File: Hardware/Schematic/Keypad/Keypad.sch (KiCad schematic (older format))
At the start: 9 parts, among them J9 Conn_01x02, U1 TCA8418RTWR

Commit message: Split-up schematics into three seperate projects with a parts library as well
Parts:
- U1: symbol TCA8418RTWR:TCA8418RTWR -> parts:TCA8418RTWR-TCA8418RTWR
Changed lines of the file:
@@
 EESchema Schematic File Version 4
-LIBS:WiFiLMR-cache
 EELAYER 29 0
 EELAYER END
 $Descr A4 11693 8268
 encoding utf-8
-Sheet 4 6
+Sheet 1 1
 Title ""
 Date ""
@@
 	2450 3200 2300 3200
 $Comp
-L TCA8418RTWR:TCA8418RTWR U?
+L parts:TCA8418RTWR-TCA8418RTWR U1
 U 1 1 5D178EB2
 P 3150 3300
-AR Path="/5D178EB2" Ref="U?"  Part="1"
+AR Path="/5D178EB2" Ref="U1"  Part="1"
 AR Path="/5D1772AD/5D178EB2" Ref="U1"  Part="1"
 F 0 "U1" H 3150 4270 50  0000 C CNN

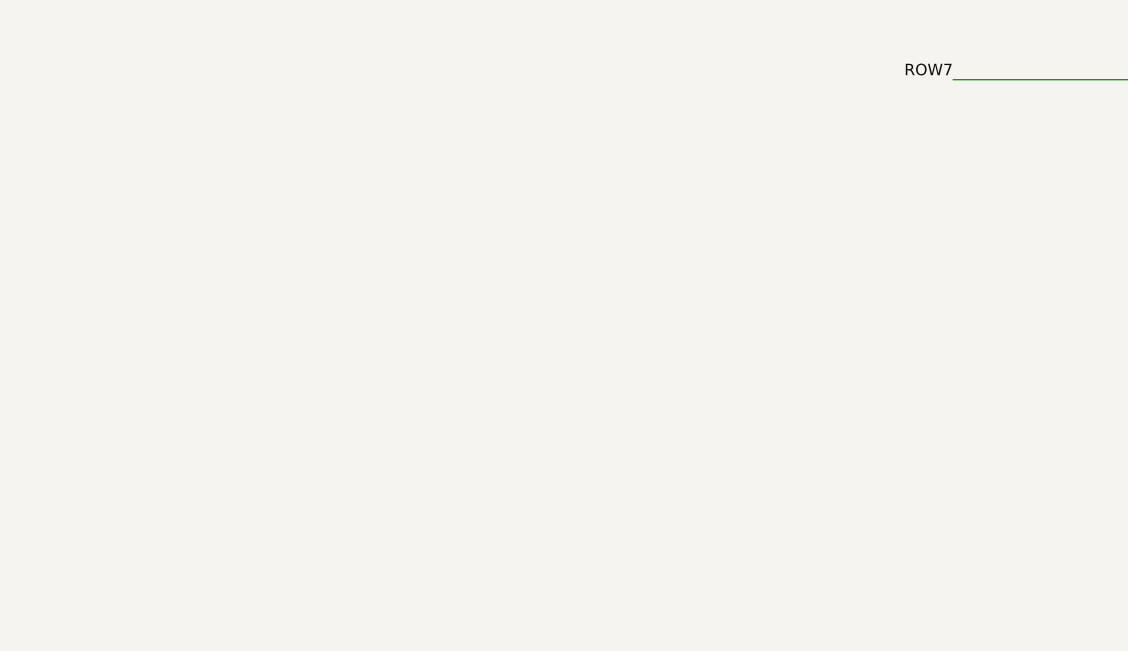
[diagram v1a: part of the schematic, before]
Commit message: Updated keypad and display schematic to use header sockets for intra-board connections.
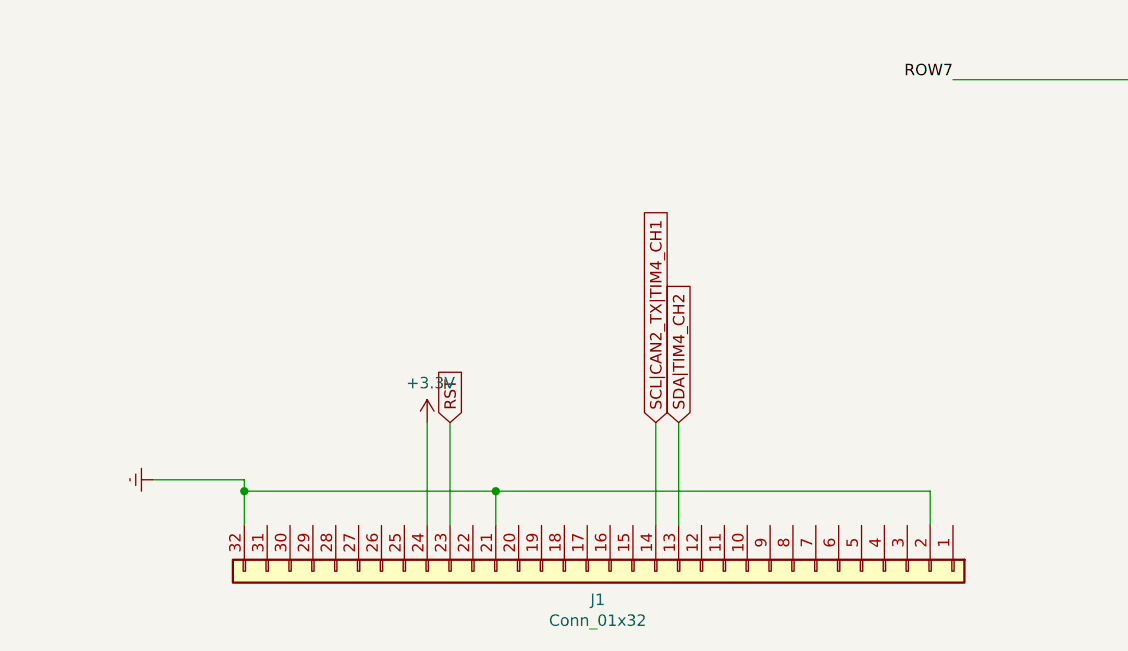
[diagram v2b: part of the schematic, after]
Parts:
- added J1: Conn_01x32, Connector_PinSocket_2.54mm:PinSocket_2x16_P2.54mm_Horizontal, symbol Connector_Generic:Conn_01x32
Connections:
- net +3V3: now also J1.24 (Pin_24)
- net Earth: now also J1.2 (Pin_2), J1.21 (Pin_21), J1.32 (Pin_32)
- net RST: now also J1.23 (Pin_23)
- net SCL|CAN2_TX|TIM4_CH1: now also J1.14 (Pin_14)
- net SDA|TIM4_CH2: now also J1.13 (Pin_13)
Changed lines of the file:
@@
 EESchema Schematic File Version 4
+LIBS:Keypad-cache
 EELAYER 29 0
 EELAYER END
@@
 Text GLabel 2300 2900 0    50   BiDi ~ 0
 RST
+$Comp
+L Connector_Generic:Conn_01x32 J1
+U 1 1 5D05A1AD
+P 3750 7350
+F 0 "J1" V 3875 7296 50  0000 C CNN
+F 1 "Conn_01x32" V 3966 7296 50  0000 C CNN
+F 2 "Connector_PinSocket_2.54mm:PinSocket_2x16_P2.54mm_Horizontal" H 3750 7350 50  0001 C CNN
+F 3 "~" H 3750 7350 50  0001 C CNN
+	1    3750 7350
+	0    1    1    0
+$EndComp
+$Comp
+L power:Earth #PWR0101
+U 1 1 5D05DF38
+P 1750 6950
+F 0 "#PWR0101" H 1750 6700 50  0001 C CNN
+F 1 "Earth" H 1750 6800 50  0001 C CNN
+F 2 "" H 1750 6950 50  0001 C CNN
+F 3 "~" H 1750 6950 50  0001 C CNN
+	1    1750 6950
+	0    1    1    0
+$EndComp
+Wire Wire Line
+	2150 7150 2150 7000
+Wire Wire Line
+	2150 6950 1750 6950
+Wire Wire Line
+	2150 7000 3250 7000
+Wire Wire Line
+	3250 7000 3250 7150
+Connection ~ 2150 7000
+Wire Wire Line
+	2150 7000 2150 6950
+Wire Wire Line
+	3250 7000 5150 7000
+Wire Wire Line
+	5150 7000 5150 7150
+Connection ~ 3250 7000
+$Comp
+L power:+3.3V #PWR0102
+U 1 1 5D061ED3
+P 2950 6700
+F 0 "#PWR0102" H 2950 6550 50  0001 C CNN
+F 1 "+3.3V" H 2965 6873 50  0000 C CNN
+F 2 "" H 2950 6700 50  0001 C CNN
+F 3 "" H 2950 6700 50  0001 C CNN
+	1    2950 6700
+	1    0    0    -1
+$EndComp
+Wire Wire Line
+	2950 7150 2950 6700
+Wire Wire Line
+	3050 7150 3050 6700
+Wire Wire Line
+	3950 7150 3950 6700
+Wire Wire Line
+	4050 7150 4050 6700
+Text GLabel 3050 6700 1    50   Input ~ 0
+RST
+Text GLabel 3950 6700 1    50   Input ~ 0
+SCL|CAN2_TX|TIM4_CH1
+Text GLabel 4050 6700 1    50   Input ~ 0
+SDA|TIM4_CH2
 $EndSCHEMATC

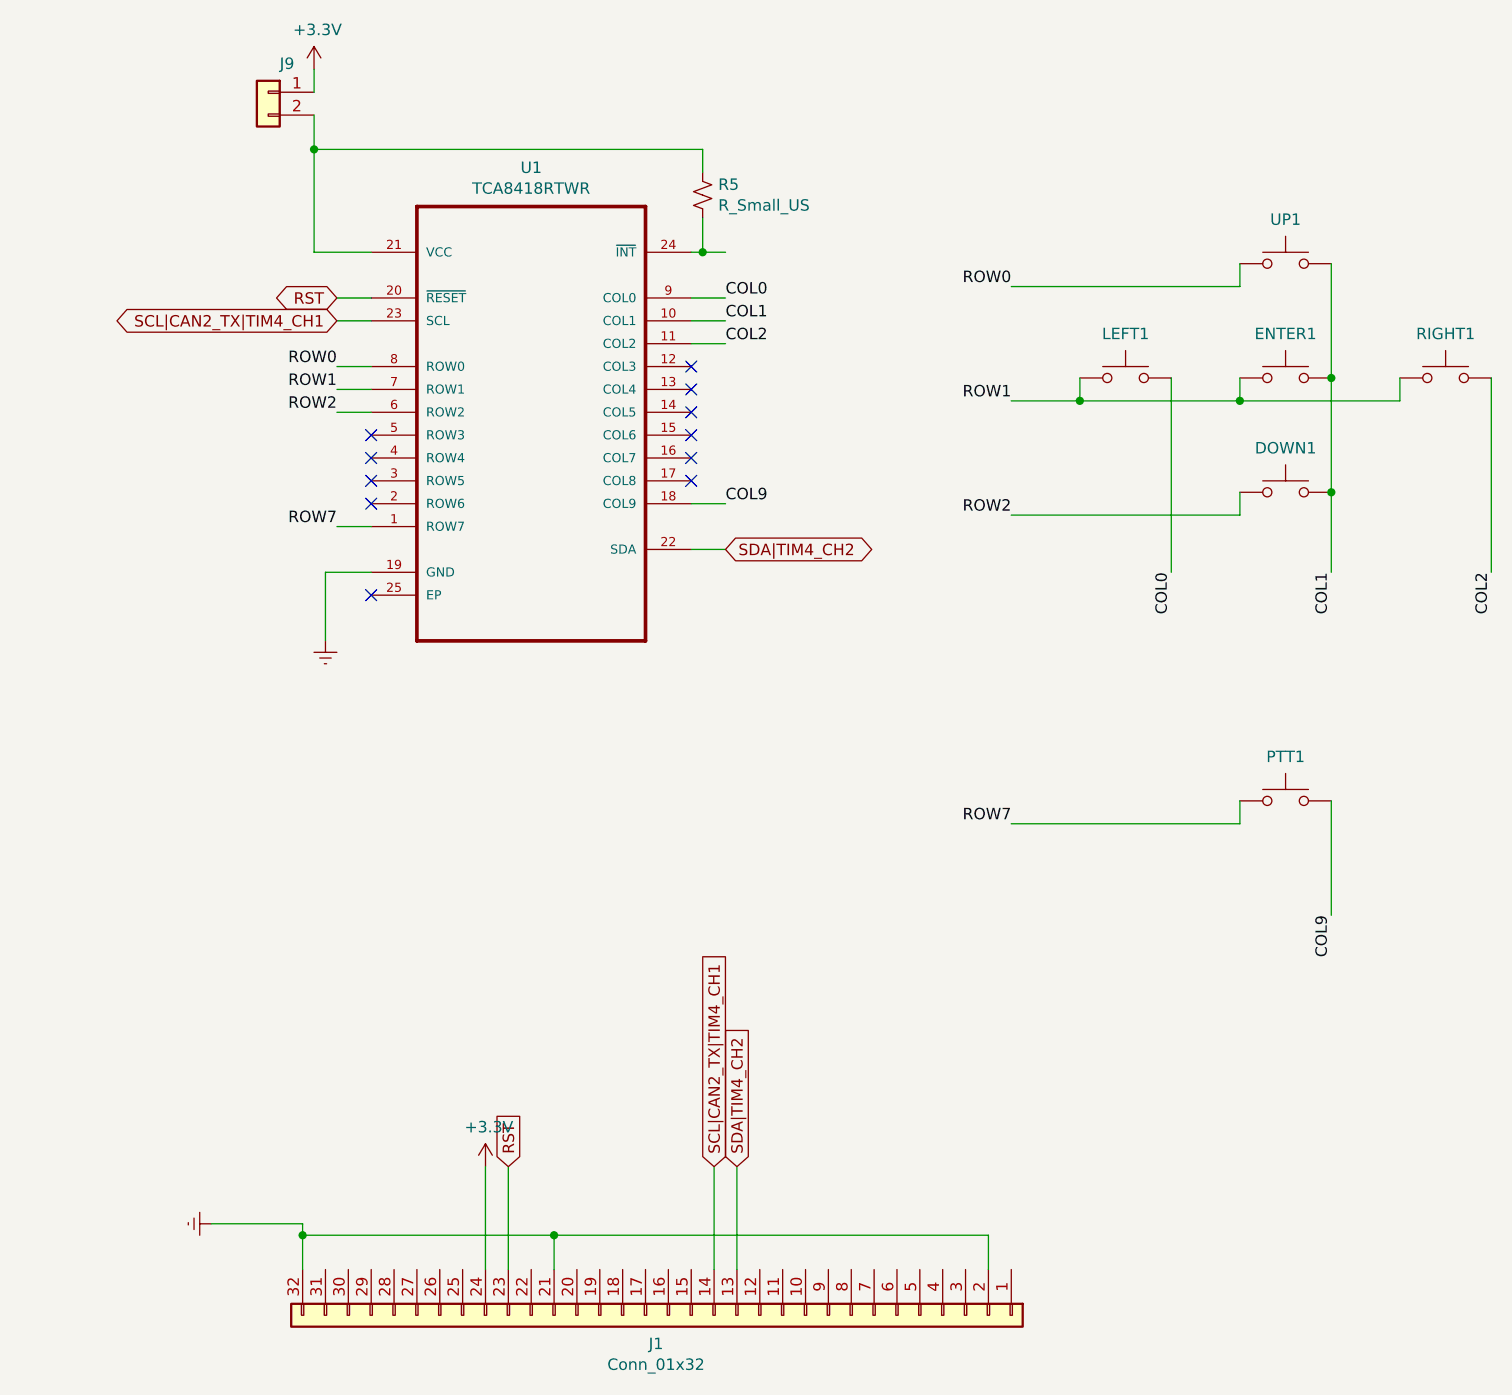
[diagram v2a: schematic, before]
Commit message: Added male 02x16 header to auxillary boards so they can be "stacked" together
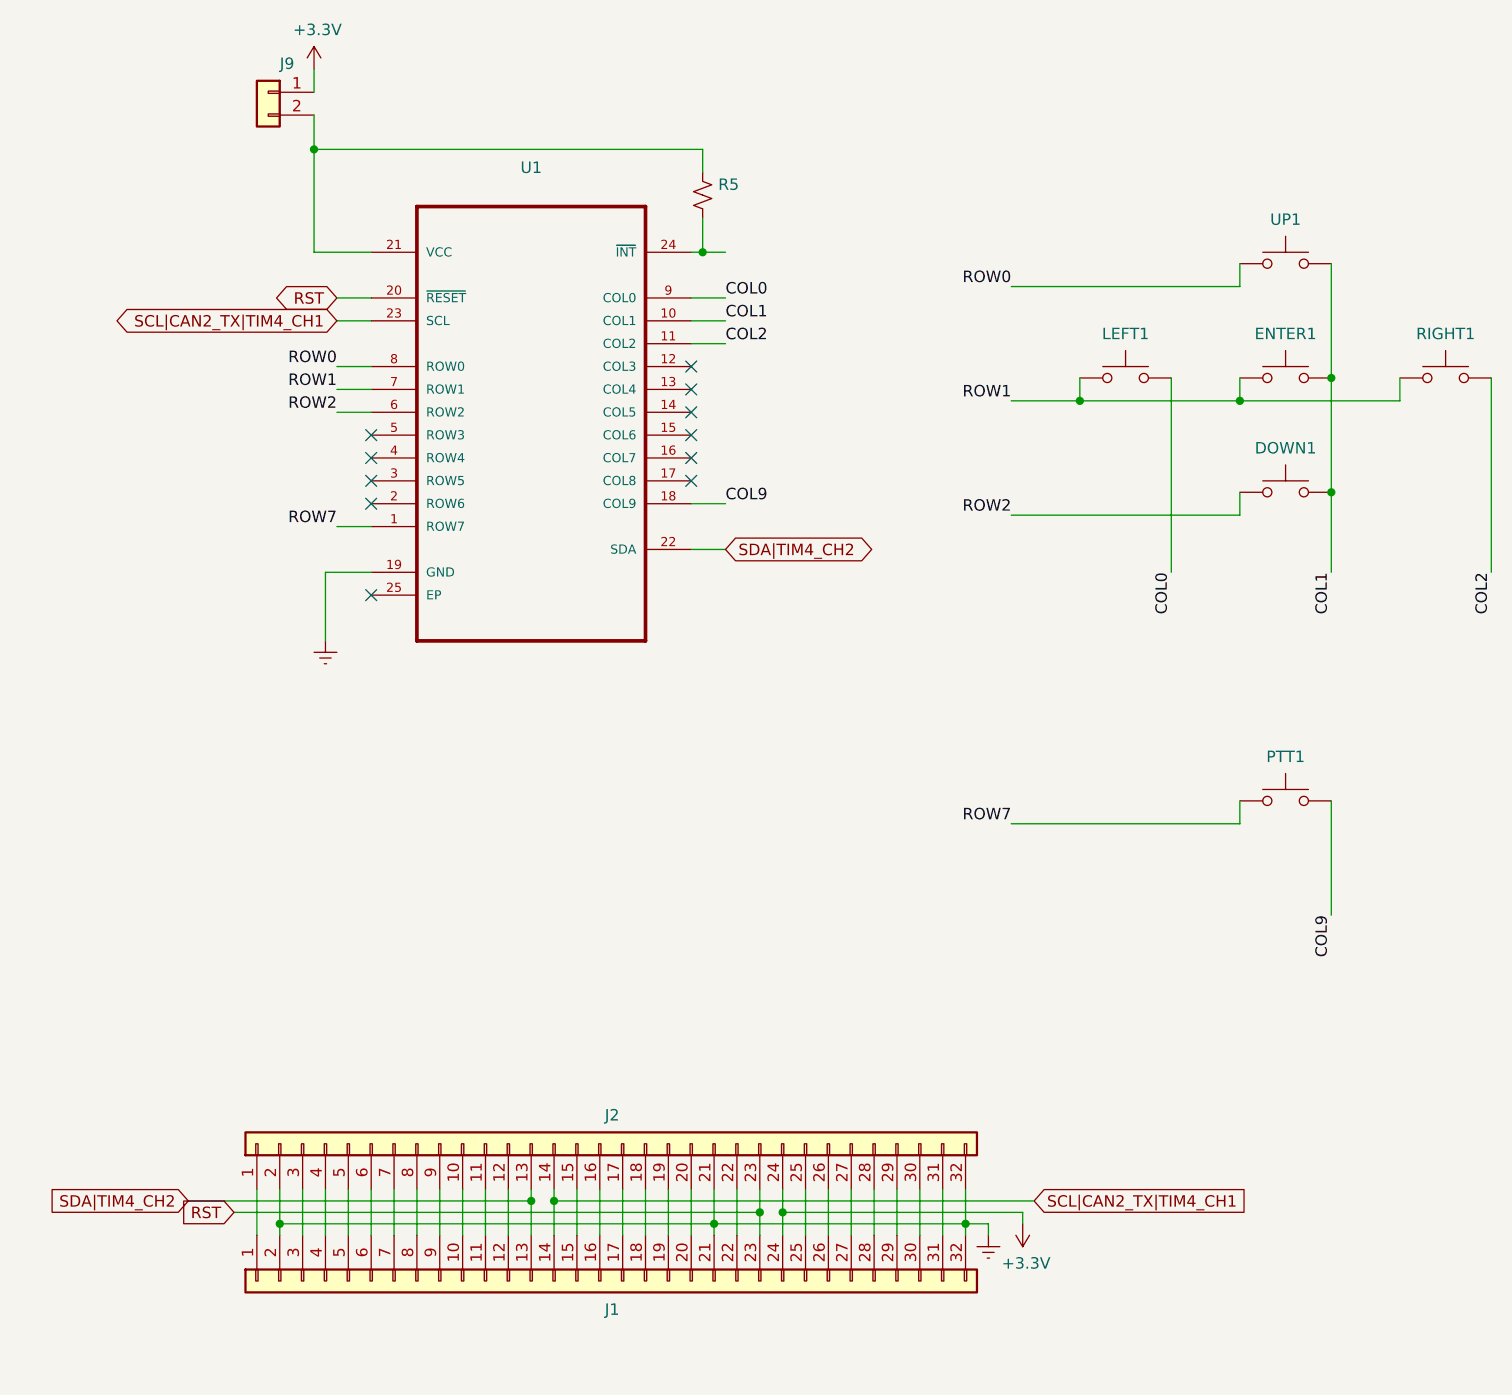
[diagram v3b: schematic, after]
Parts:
- added J2: Conn_01x32, Connector_PinHeader_2.54mm:PinHeader_2x16_P2.54mm_Horizontal, symbol Connector_Generic:Conn_01x32
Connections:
- net +3V3: now also J2.24 (Pin_24)
- net Earth: now also J2.2 (Pin_2), J2.21 (Pin_21), J2.32 (Pin_32)
- net RST: now also J2.23 (Pin_23)
- net SCL|CAN2_TX|TIM4_CH1: now also J2.14 (Pin_14)
- net SDA|TIM4_CH2: now also J2.13 (Pin_13)
- net at J1.1 (Pin_1): now also J2.1 (Pin_1)
- net at J1.10 (Pin_10): now also J2.10 (Pin_10)
- net at J1.11 (Pin_11): now also J2.11 (Pin_11)
- net at J1.12 (Pin_12): now also J2.12 (Pin_12)
- net at J1.15 (Pin_15): now also J2.15 (Pin_15)
- net at J1.16 (Pin_16): now also J2.16 (Pin_16)
- net at J1.17 (Pin_17): now also J2.17 (Pin_17)
- net at J1.18 (Pin_18): now also J2.18 (Pin_18)
- net at J1.19 (Pin_19): now also J2.19 (Pin_19)
- net at J1.20 (Pin_20): now also J2.20 (Pin_20)
- net at J1.22 (Pin_22): now also J2.22 (Pin_22)
- net at J1.25 (Pin_25): now also J2.25 (Pin_25)
- net at J1.26 (Pin_26): now also J2.26 (Pin_26)
- net at J1.27 (Pin_27): now also J2.27 (Pin_27)
- net at J1.28 (Pin_28): now also J2.28 (Pin_28)
- net at J1.29 (Pin_29): now also J2.29 (Pin_29)
- net at J1.3 (Pin_3): now also J2.3 (Pin_3)
- net at J1.30 (Pin_30): now also J2.30 (Pin_30)
- net at J1.31 (Pin_31): now also J2.31 (Pin_31)
- net at J1.4 (Pin_4): now also J2.4 (Pin_4)
- net at J1.5 (Pin_5): now also J2.5 (Pin_5)
- net at J1.6 (Pin_6): now also J2.6 (Pin_6)
- net at J1.7 (Pin_7): now also J2.7 (Pin_7)
- net at J1.8 (Pin_8): now also J2.8 (Pin_8)
- net at J1.9 (Pin_9): now also J2.9 (Pin_9)
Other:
- moved on the sheet: J1
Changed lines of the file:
@@
 P 3900 2450
 F 0 "R5" H 3968 2496 50  0000 L CNN
-F 1 "R_Small_US" H 3968 2405 50  0000 L CNN
+F 1 "R_Small_US" H 3968 2405 50  0001 L CNN
 F 2 "Resistor_SMD:R_2512_6332Metric_Pad1.52x3.35mm_HandSolder" H 3900 2450 50  0001 C CNN
 F 3 "~" H 3900 2450 50  0001 C CNN
@@
 AR Path="/5D1772AD/5D178EB2" Ref="U1"  Part="1"
 F 0 "U1" H 3150 4270 50  0000 C CNN
-F 1 "TCA8418RTWR" H 3150 4179 50  0000 C CNN
+F 1 "TCA8418RTWR" H 3150 4179 50  0001 C CNN
 F 2 "QFN50P400X400X80-25N" H 3150 3300 50  0001 L BNN
 F 3 "" H 3150 3300 50  0001 L BNN
@@
 Text GLabel 2300 2900 0    50   BiDi ~ 0
 RST
+Text GLabel 1850 6900 0    50   Input ~ 0
+RST
+Text GLabel 1650 6850 0    50   Input ~ 0
+SDA|TIM4_CH2
+Wire Wire Line
+	2050 6950 2050 7000
+Wire Wire Line
+	3950 6950 3950 7000
+Connection ~ 5050 6950
+$Comp
+L Connector_Generic:Conn_01x32 J2
+U 1 1 5D08D824
+P 3450 6600
+F 0 "J2" V 3575 6546 50  0000 C CNN
+F 1 "Conn_01x32" H 3368 8226 50  0001 C CNN
+F 2 "Connector_PinHeader_2.54mm:PinHeader_2x16_P2.54mm_Horizontal" H 3450 6600 50  0001 C CNN
+F 3 "~" H 3450 6600 50  0001 C CNN
+	1    3450 6600
+	0    -1   -1   0
+$EndComp
+$Comp
+L power:+3.3V #PWR0102
+U 1 1 5D061ED3
+P 5300 6950
+F 0 "#PWR0102" H 5300 6800 50  0001 C CNN
+F 1 "+3.3V" H 5315 7123 50  0000 C CNN
+F 2 "" H 5300 6950 50  0001 C CNN
+F 3 "" H 5300 6950 50  0001 C CNN
+	1    5300 6950
+	1    0    0    1
+$EndComp
+Wire Wire Line
+	5050 6950 5150 6950
+Wire Wire Line
+	5050 7000 5050 6950
+$Comp
+L power:Earth #PWR0101
+U 1 1 5D05DF38
+P 5150 7000
+F 0 "#PWR0101" H 5150 6750 50  0001 C CNN
+F 1 "Earth" H 5150 6850 50  0001 C CNN
+F 2 "" H 5150 7000 50  0001 C CNN
+F 3 "~" H 5150 7000 50  0001 C CNN
+	1    5150 7000
+	-1   0    0    -1
+$EndComp
+Wire Wire Line
+	1850 6900 4150 6900
 $Comp
 L Connector_Generic:Conn_01x32 J1
 U 1 1 5D05A1AD
-P 3750 7350
-F 0 "J1" V 3875 7296 50  0000 C CNN
-F 1 "Conn_01x32" V 3966 7296 50  0000 C CNN
-F 2 "Connector_PinSocket_2.54mm:PinSocket_2x16_P2.54mm_Horizontal" H 3750 7350 50  0001 C CNN
-F 3 "~" H 3750 7350 50  0001 C CNN
-	1    3750 7350
-	0    1    1    0
-$EndComp
-$Comp
-L power:Earth #PWR0101
-U 1 1 5D05DF38
-P 1750 6950
-F 0 "#PWR0101" H 1750 6700 50  0001 C CNN
-F 1 "Earth" H 1750 6800 50  0001 C CNN
-F 2 "" H 1750 6950 50  0001 C CNN
-F 3 "~" H 1750 6950 50  0001 C CNN
-	1    1750 6950
-	0    1    1    0
-$EndComp
-Wire Wire Line
-	2150 7150 2150 7000
-Wire Wire Line
-	2150 6950 1750 6950
-Wire Wire Line
-	2150 7000 3250 7000
-Wire Wire Line
-	3250 7000 3250 7150
-Connection ~ 2150 7000
-Wire Wire Line
-	2150 7000 2150 6950
-Wire Wire Line
-	3250 7000 5150 7000
-Wire Wire Line
-	5150 7000 5150 7150
-Connection ~ 3250 7000
-$Comp
-L power:+3.3V #PWR0102
-U 1 1 5D061ED3
-P 2950 6700
-F 0 "#PWR0102" H 2950 6550 50  0001 C CNN
-F 1 "+3.3V" H 2965 6873 50  0000 C CNN
-F 2 "" H 2950 6700 50  0001 C CNN
-F 3 "" H 2950 6700 50  0001 C CNN
-	1    2950 6700
-	1    0    0    -1
-$EndComp
-Wire Wire Line
-	2950 7150 2950 6700
-Wire Wire Line
-	3050 7150 3050 6700
-Wire Wire Line
-	3950 7150 3950 6700
-Wire Wire Line
-	4050 7150 4050 6700
-Text GLabel 3050 6700 1    50   Input ~ 0
-RST
-Text GLabel 3950 6700 1    50   Input ~ 0
+P 3450 7200
+F 0 "J1" V 3575 7146 50  0000 C CNN
+F 1 "Conn_01x32" V 3666 7146 50  0001 C CNN
+F 2 "Connector_PinSocket_2.54mm:PinSocket_2x16_P2.54mm_Horizontal" H 3450 7200 50  0001 C CNN
+F 3 "~" H 3450 7200 50  0001 C CNN
+	1    3450 7200
+	0    -1   1    0
+$EndComp
+Wire Wire Line
+	3950 6950 2050 6950
+Connection ~ 3950 6950
+Wire Wire Line
+	4250 7000 4250 6900
+Wire Wire Line
+	4150 7000 4150 6900
+Wire Wire Line
+	5050 6950 3950 6950
+Text GLabel 5350 6850 2    50   Input ~ 0
 SCL|CAN2_TX|TIM4_CH1
-Text GLabel 4050 6700 1    50   Input ~ 0
-SDA|TIM4_CH2
+Wire Wire Line
+	3150 6850 3150 7000
+Wire Wire Line
+	3150 6850 3150 6800
+Connection ~ 3150 6850
+Wire Wire Line
+	2050 6950 2050 6800
+Connection ~ 2050 6950
+Wire Wire Line
+	1950 7000 1950 6800
+Wire Wire Line
+	2150 7000 2150 6800
+Wire Wire Line
+	2250 7000 2250 6800
+Wire Wire Line
+	2350 7000 2350 6800
+Wire Wire Line
+	2450 7000 2450 6800
+Wire Wire Line
+	2550 7000 2550 6800
+Wire Wire Line
+	2650 6800 2650 7000
+Wire Wire Line
+	2750 7000 2750 6800
+Wire Wire Line
+	2850 7000 2850 6800
+Wire Wire Line
+	2950 7000 2950 6800
+Wire Wire Line
+	3050 7000 3050 6800
+Wire Wire Line
+	3350 7000 3350 6800
+Wire Wire Line
+	3450 7000 3450 6800
+Wire Wire Line
+	3550 7000 3550 6800
+Wire Wire Line
+	3650 7000 3650 6800
+Wire Wire Line
+	3750 7000 3750 6800
+Wire Wire Line
+	3850 7000 3850 6800
+Wire Wire Line
+	4050 7000 4050 6800
+Wire Wire Line
+	3950 6950 3950 6800
+Wire Wire Line
+	4250 6900 4250 6800
+Connection ~ 4250 6900
+Wire Wire Line
+	4150 6900 4150 6800
+Connection ~ 4150 6900
+Wire Wire Line
+	4350 7000 4350 6800
+Wire Wire Line
+	4450 7000 4450 6800
+Wire Wire Line
+	4550 7000 4550 6800
+Wire Wire Line
+	4650 6800 4650 7000
+Wire Wire Line
+	4750 7000 4750 6800
+Wire Wire Line
+	4850 6800 4850 7000
+Wire Wire Line
+	4950 6800 4950 7000
+Wire Wire Line
+	5050 6950 5050 6800
+Wire Wire Line
+	1650 6850 3150 6850
+Wire Wire Line
+	5150 6950 5150 7000
+Wire Wire Line
+	5300 6900 5300 6950
+Wire Wire Line
+	4250 6900 5300 6900
+Wire Wire Line
+	3250 6800 3250 6850
+Wire Wire Line
+	3250 6850 5350 6850
+Connection ~ 3250 6850
+Wire Wire Line
+	3250 6850 3250 7000
 $EndSCHEMATC
